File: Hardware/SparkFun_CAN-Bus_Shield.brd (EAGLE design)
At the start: 53.3 x 59.7 mm, 48 parts, among them Q1 16MHz, U1 USD-SOCKETNEW, U2 ARDUINO_R3_SHIELD, U3 JST_VERTICAL, U4 MCP2515, U5 MCP2551, U6 HEX_CONVERTER, X1 DB9 Plug

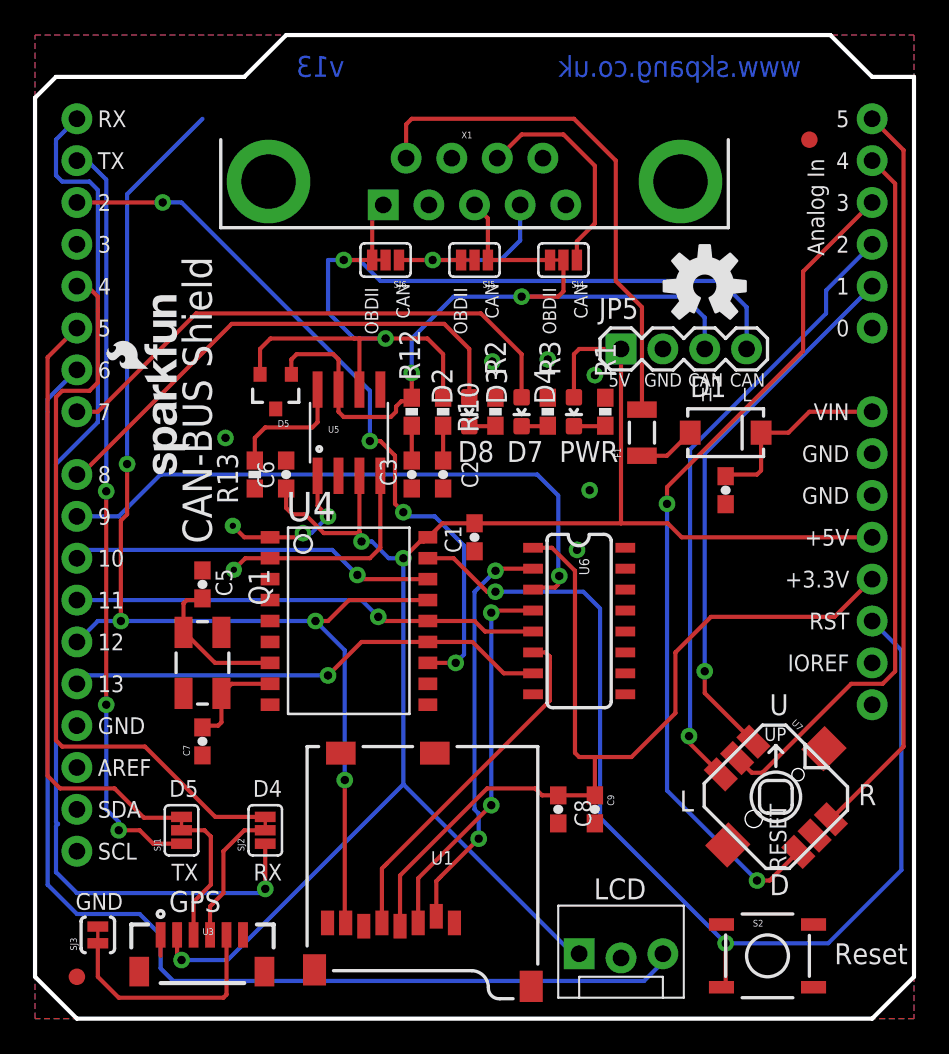
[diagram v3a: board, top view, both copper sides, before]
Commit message: Adding in feedback from Sukkin, and engineering review/QC checklist
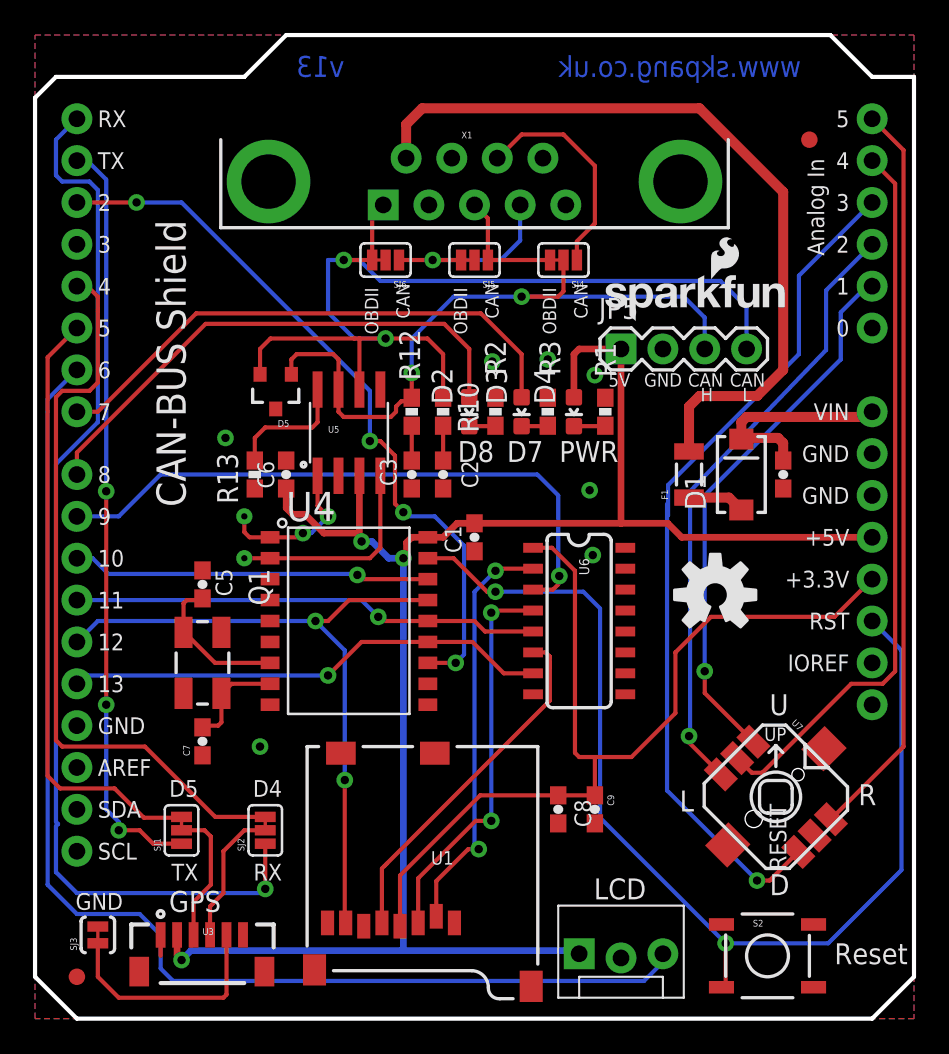
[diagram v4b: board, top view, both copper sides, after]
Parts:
- moved JP4 26.5 mm to (34.2, 42.2), turned to 0 degrees
- moved LOGO1 18.7 mm to (41.3, 25.7)
- moved F1 3.82 mm to (39.7, 33.0)
- moved C4 3.62 mm to (45.4, 33.0)
- moved D1 2.71 mm to (42.9, 33.0), turned to 90 degrees
- moved TP1 0.94 mm to (12.7, 27.9)
- moved TP2 0.90 mm to (12.7, 30.5)
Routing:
- net MISO: track 74.0 -> 41.4 mm, vias 4 -> 2
- net N$13: track 31.7 -> 47.6 mm
- net VCC: track 107.7 -> 109.7 mm
- net 12V: track 11.9 -> 13.0 mm
- net CAN_RXD: track 13.8 -> 12.9 mm
- net LED1: track 31.2 -> 31.9 mm
- net JOY-DOWN: track 51.8 -> 52.6 mm, vias 2 -> 1
- net N$19: track 23.3 -> 23.8 mm
- net GND: vias 6 -> 7

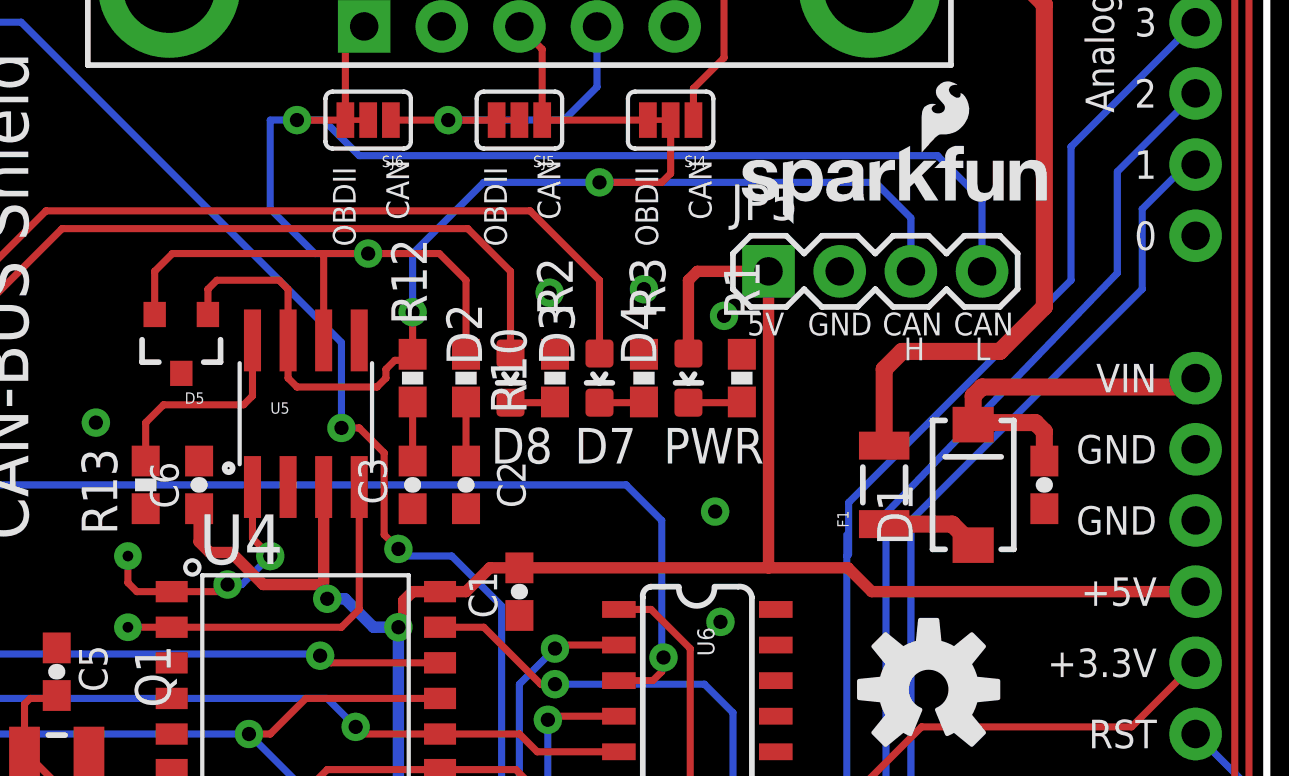
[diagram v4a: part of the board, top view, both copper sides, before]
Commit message: Fixing DRC errors
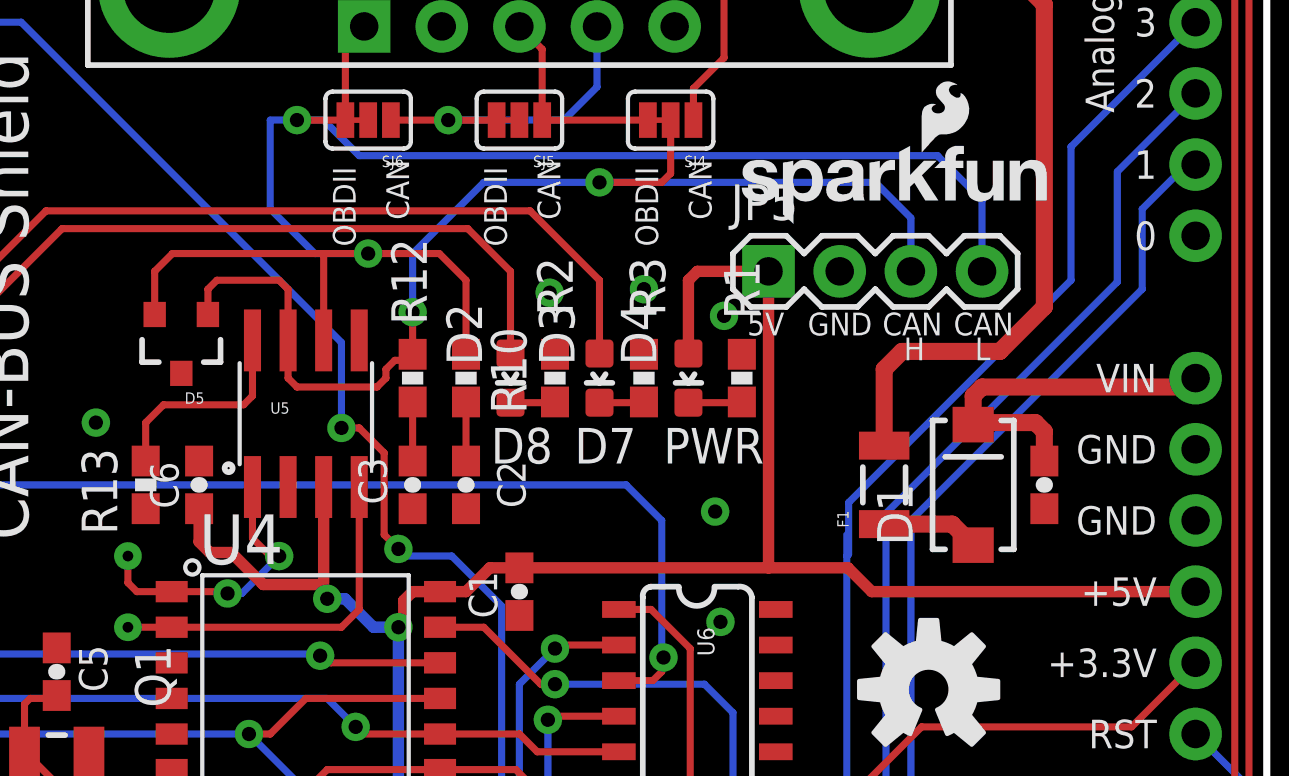
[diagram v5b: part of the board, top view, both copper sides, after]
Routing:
- net CAN_TXD: track 9.42 -> 10.1 mm
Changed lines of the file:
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@@
 <contactref element="U5" pad="1"/>
 <contactref element="U4" pad="1"/>
-<wire x1="16.256" y1="29.464" x2="16.764" y2="29.464" width="0.254" layer="16"/>
-<wire x1="16.764" y1="29.464" x2="17.78" y2="30.48" width="0.254" layer="16"/>
-<wire x1="14.2621" y1="29.21" x2="16.002" y2="29.21" width="0.254" layer="1"/>
-<wire x1="16.002" y1="29.21" x2="16.256" y2="29.464" width="0.254" layer="1"/>
-<via x="16.256" y="29.464" extent="1-16" drill="0.508"/>
-<via x="17.78" y="30.48" extent="1-16" drill="0.508"/>
+<via x="16.256" y="29.1465" extent="1-16" drill="0.508"/>
+<via x="18.0975" y="30.48" extent="1-16" drill="0.508"/>
 <wire x1="17.145" y1="32.9438" x2="17.145" y2="31.115" width="0.254" layer="1"/>
-<wire x1="17.145" y1="31.115" x2="17.78" y2="30.48" width="0.254" layer="1"/>
 <contactref element="TP2" pad="P$1"/>
 <wire x1="14.2621" y1="29.21" x2="13.0175" y2="29.21" width="0.254" layer="1"/>
 <wire x1="13.0175" y1="29.21" x2="12.7" y2="29.5275" width="0.254" layer="1"/>
 <wire x1="12.7" y1="29.5275" x2="12.7" y2="30.48" width="0.254" layer="1"/>
+<wire x1="14.2621" y1="29.21" x2="16.1925" y2="29.21" width="0.254" layer="1"/>
+<wire x1="16.1925" y1="29.21" x2="16.256" y2="29.1465" width="0.254" layer="1"/>
+<wire x1="18.0975" y1="30.48" x2="17.78" y2="30.48" width="0.254" layer="1"/>
+<wire x1="17.78" y1="30.48" x2="17.145" y2="31.115" width="0.254" layer="1"/>
+<wire x1="16.256" y1="29.1465" x2="16.764" y2="29.1465" width="0.254" layer="16"/>
+<wire x1="16.764" y1="29.1465" x2="18.0975" y2="30.48" width="0.254" layer="16"/>
 </signal>
 <signal name="N$9">
@@
 <contactref element="U7" pad="C"/>
 <wire x1="39.751" y1="17.2085" x2="39.751" y2="32.004" width="0.254" layer="16"/>
-<wire x1="39.751" y1="32.004" x2="48.006" y2="40.5765" width="0.254" layer="16"/>
 <wire x1="48.006" y1="44.196" x2="50.8" y2="46.99" width="0.254" layer="16"/>
-<wire x1="48.006" y1="40.5765" x2="48.006" y2="44.196" width="0.254" layer="16"/>
 <wire x1="39.751" y1="17.2085" x2="39.6875" y2="17.145" width="0.254" layer="16"/>
 <via x="39.6875" y="17.145" extent="1-16" drill="0.508"/>
 <wire x1="39.6875" y1="17.145" x2="39.6875" y2="16.752596875" width="0.254" layer="1"/>
 <wire x1="39.6875" y1="16.752596875" x2="41.61691875" y2="14.823178125" width="0.254" layer="1"/>
+<wire x1="48.006" y1="44.196" x2="48.006" y2="40.259" width="0.254" layer="16"/>
+<wire x1="48.006" y1="40.259" x2="39.751" y2="32.004" width="0.254" layer="16"/>
 </signal>
 <signal name="JOY-DOWN">

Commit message: Pushing QC checklist changes
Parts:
- TP1, TP2: value TEST-POINTTP_15TH_THRU -> TEST-POINT3X5; device SparkFun-Passives:TP_15TH -> SparkFun-Passives:PAD.03X.05
- moved R13 4.02 mm to (12.1, 36.8), turned to 270 degrees
- moved C1 0.63 mm to (26.7, 29.8), turned to 270 degrees
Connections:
- net VCC renamed 5V
- net GND: now also D5.3
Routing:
- net 3.3V: track 58.2 -> 52.7 mm
- net RS: track 66.3 -> 64.0 mm
- net CANL: track 57.4 -> 55.9 mm
- net CAN_TXD: track 10.1 -> 9.28 mm
- net N$18: track 9.08 -> 9.87 mm

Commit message: Fixing test points
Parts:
- flipped TP1 to the bottom
- flipped TP2 to the bottom
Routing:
- net CAN_RXD: track 12.9 -> 16.4 mm, vias 0 -> 1
- net CAN_TXD: track 9.28 -> 10.9 mm
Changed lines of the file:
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@@
 <setting verticaltext="up"/>
 </settings>
-<grid distance="0.0125" unitdist="inch" unit="inch" style="lines" multiple="1" display="yes" altdistance="0.005" altunitdist="inch" altunit="inch"/>
+<grid distance="0.05" unitdist="inch" unit="inch" style="lines" multiple="1" display="yes" altdistance="0.005" altunitdist="inch" altunit="inch"/>
 <layers>
 <layer number="1" name="Top" color="4" fill="1" visible="yes" active="yes"/>
@@
 <layer number="47" name="Measures" color="7" fill="1" visible="no" active="yes"/>
 <layer number="48" name="Document" color="7" fill="1" visible="no" active="yes"/>
-<layer number="49" name="Reference" color="7" fill="1" visible="yes" active="yes"/>
+<layer number="49" name="Reference" color="7" fill="1" visible="no" active="yes"/>
 <layer number="50" name="dxf" color="7" fill="1" visible="no" active="yes"/>
 <layer number="51" name="tDocu" color="6" fill="1" visible="yes" active="yes"/>
@@
 <element name="LOGO1" library="SparkFun-Aesthetics" package="OSHW-LOGO-M" value="OSHW-LOGOM" x="41.275" y="25.7175"/>
 <element name="SJ3" library="SparkFun-Passives" package="PAD-JUMPER-2-NC_BY_TRACE_YES_SILK" value="JUMPER-PAD-2-NC_BY_TRACE" x="3.81" y="5.08" rot="R90"/>
-<element name="TP1" library="SparkFun-Passives" package="PAD.03X.05" value="TEST-POINT3X5" x="12.7" y="27.94"/>
-<element name="TP2" library="SparkFun-Passives" package="PAD.03X.05" value="TEST-POINT3X5" x="12.7" y="30.48"/>
+<element name="TP1" library="SparkFun-Passives" package="PAD.03X.05" value="TEST-POINT3X5" x="12.7" y="27.94" rot="MR0"/>
+<element name="TP2" library="SparkFun-Passives" package="PAD.03X.05" value="TEST-POINT3X5" x="12.7" y="30.48" rot="MR0"/>
 <element name="FRAME2" library="SparkFun-Aesthetics" package="DUMMY" value="" x="-11.43" y="-25.4">
 <attribute name="VERSION" value="v13" x="-11.43" y="-25.4" size="1.778" layer="27" font="vector" ratio="15" display="off"/>
@@
 <contactref element="U5" pad="4"/>
 <contactref element="U4" pad="2"/>
-<wire x1="14.2621" y1="27.94" x2="20.32" y2="27.94" width="0.254" layer="1"/>
+<wire x1="17.78" y1="27.94" x2="20.32" y2="27.94" width="0.254" layer="1"/>
 <wire x1="20.955" y1="28.575" x2="20.955" y2="32.9438" width="0.254" layer="1"/>
 <wire x1="20.955" y1="28.575" x2="20.32" y2="27.94" width="0.254" layer="1"/>
 <contactref element="TP1" pad="P$1"/>
-<wire x1="14.2621" y1="27.94" x2="12.7" y2="27.94" width="0.254" layer="1"/>
+<wire x1="12.7" y1="27.94" x2="17.78" y2="27.94" width="0.254" layer="16"/>
+<via x="17.78" y="27.94" extent="1-16" drill="0.508"/>
+<wire x1="17.78" y1="27.94" x2="14.2621" y2="27.94" width="0.254" layer="1"/>
 </signal>
 <signal name="CAN_TXD">
@@
 <via x="16.51" y="30.7975" extent="1-16" drill="0.508"/>
 <contactref element="TP2" pad="P$1"/>
-<wire x1="14.2621" y1="29.21" x2="13.0175" y2="29.21" width="0.254" layer="1"/>
-<wire x1="13.0175" y1="29.21" x2="12.7" y2="29.5275" width="0.254" layer="1"/>
-<wire x1="12.7" y1="29.5275" x2="12.7" y2="30.48" width="0.254" layer="1"/>
 <wire x1="14.2621" y1="29.21" x2="15.875" y2="29.21" width="0.254" layer="1"/>
 <wire x1="15.875" y1="29.21" x2="16.256" y2="28.829" width="0.254" layer="1"/>
@@
 <wire x1="16.51" y1="30.7975" x2="16.51" y2="29.083" width="0.254" layer="16"/>
 <wire x1="16.51" y1="29.083" x2="16.256" y2="28.829" width="0.254" layer="16"/>
+<wire x1="16.256" y1="28.829" x2="14.351" y2="28.829" width="0.254" layer="16"/>
+<wire x1="14.351" y1="28.829" x2="12.7" y2="30.48" width="0.254" layer="16"/>
 </signal>
 <signal name="N$9">

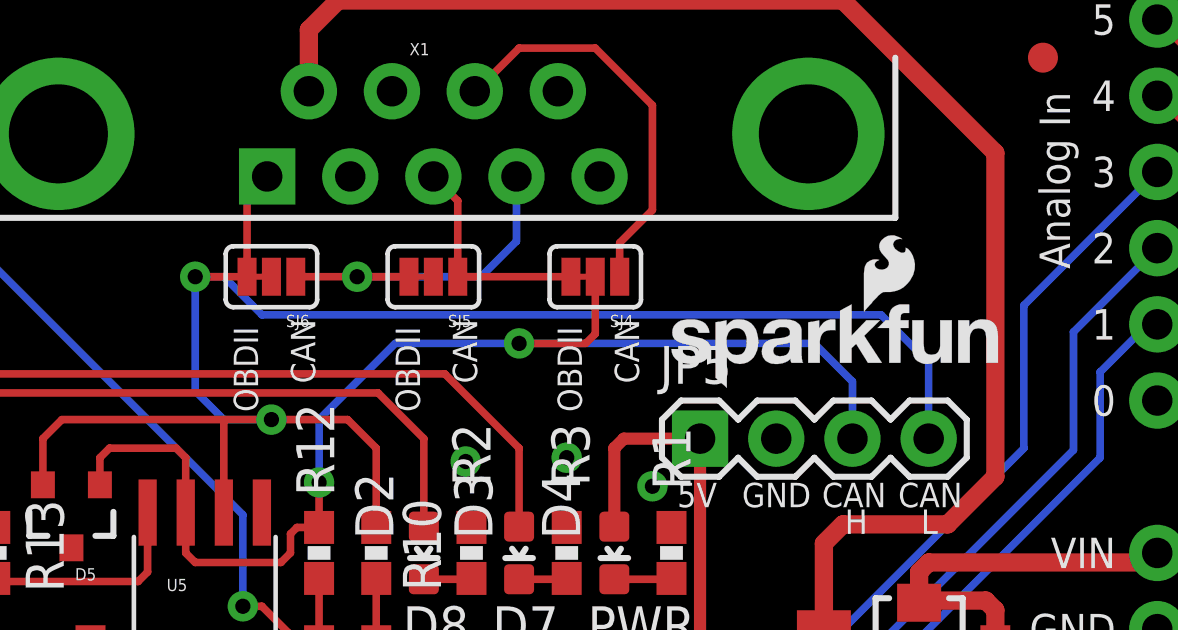
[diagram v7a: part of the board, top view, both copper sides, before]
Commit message: Added production directory, updating shield units to pass QC check
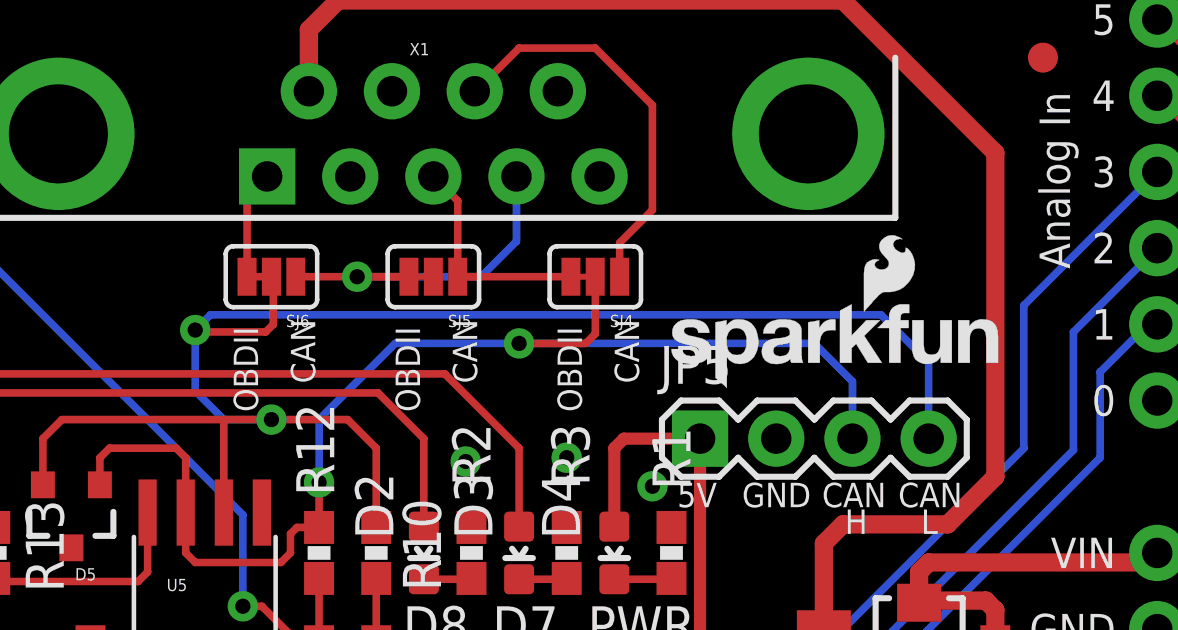
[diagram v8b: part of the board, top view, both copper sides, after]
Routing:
- net CANL: track 55.9 -> 56.9 mm
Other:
- board text added: "Units: inches"
